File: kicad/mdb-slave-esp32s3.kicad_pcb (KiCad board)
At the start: 2 copper layers, 39 x 41 mm, 39 parts, among them J1 MDB_Connector, J2 USB_C_Receptacle_USB2.0_16P, J3 Conn_02x11_Odd_Even, SW1 SW_Push, U1 TLP785, U3 ESP32-S3FH4R2, U4 TLP785, U5 LM2594HVM-3.3, Y1 Crystal_GND24

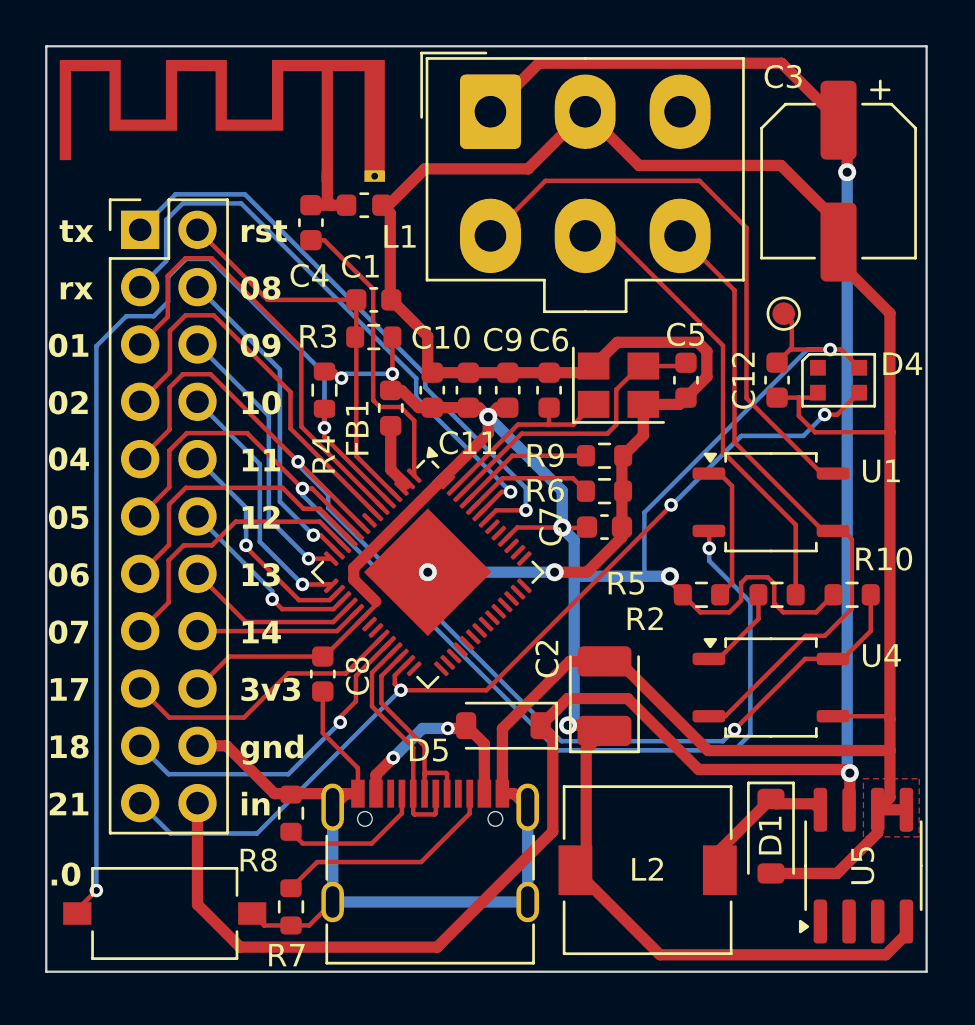
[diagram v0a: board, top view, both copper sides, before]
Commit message: Refacting vias/wifi line
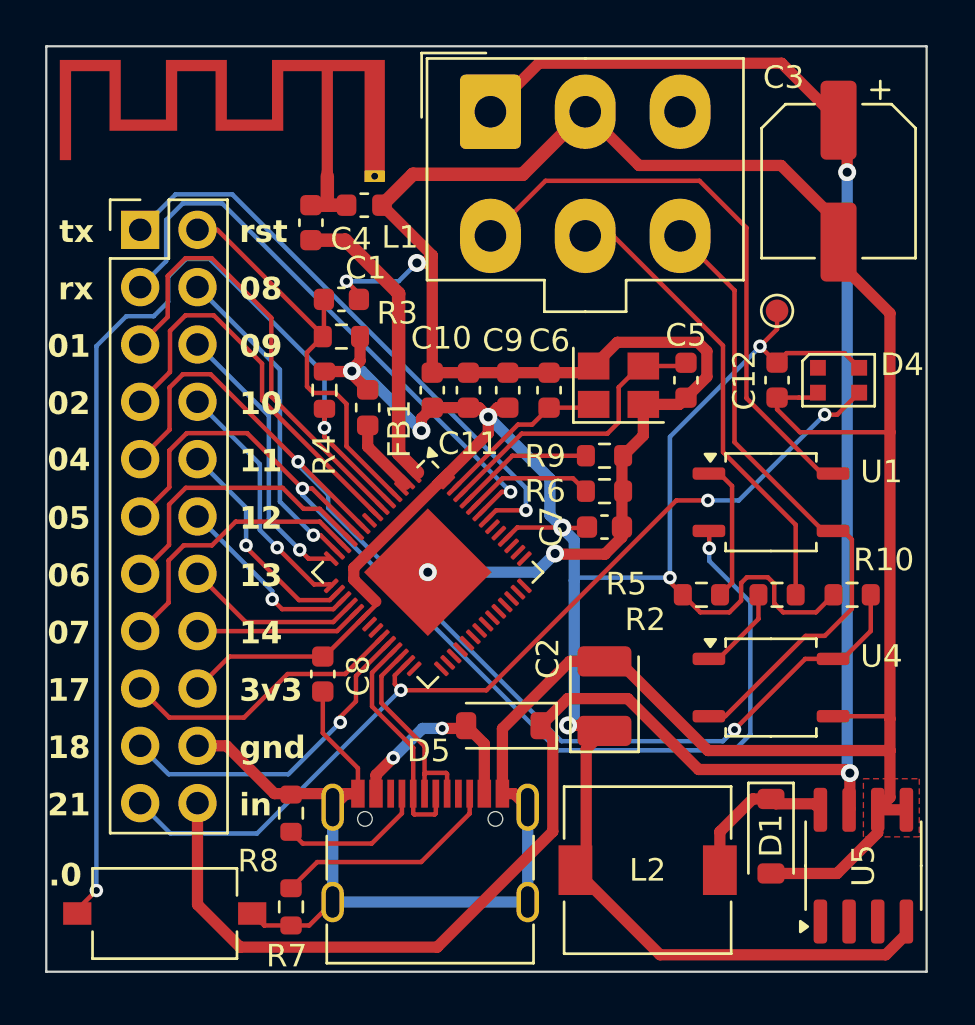
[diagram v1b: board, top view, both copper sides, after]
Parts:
- moved C1 1.44 mm to (181.6, 94.3)
- moved R3 1.44 mm to (181.6, 96.0)
- moved FB1 1.02 mm to (182.7, 99.1)
- moved TP4 0.32 mm to (200.9, 94.8)
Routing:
- net GND: track 169.8 -> 175.9 mm, vias 2 -> 4
- net /reset: track 17.7 -> 18.7 mm
- net Net-(U3-XTAL_P): track 8.49 -> 7.72 mm
- net +3V3: track 112.2 -> 112.8 mm
